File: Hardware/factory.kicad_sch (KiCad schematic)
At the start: 10 parts, among them P1 Mains_Connector, SW1 Timer_Switch, SW2 Setting_Switch, SW3 Both_Heaters

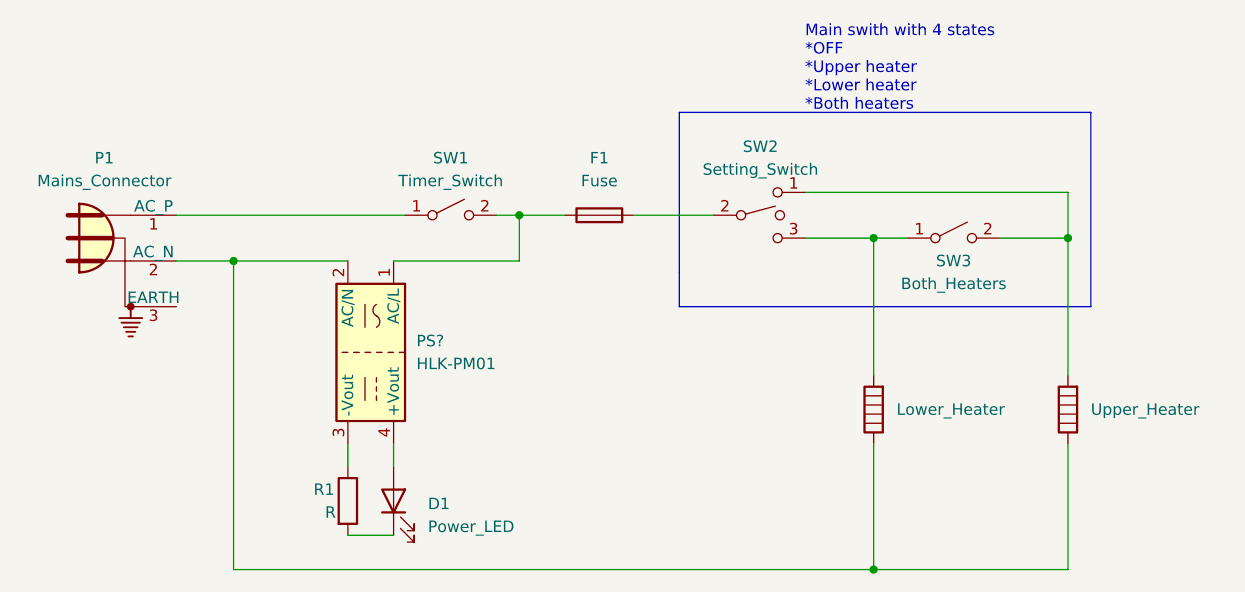
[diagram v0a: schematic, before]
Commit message: Electrical schematic functionally complete, not added fuse rating
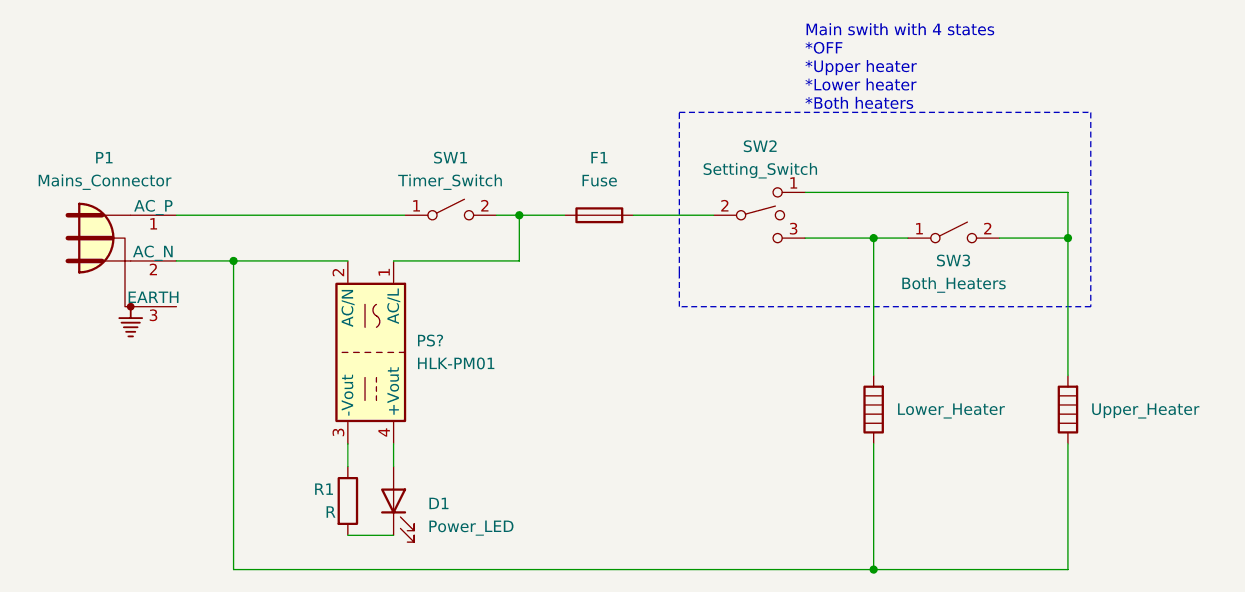
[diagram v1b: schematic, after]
